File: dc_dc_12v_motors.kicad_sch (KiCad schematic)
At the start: 18 parts, among them Q7 CSD17505Q5A, Q8 CSD18540Q5B, U8 LM3150MH

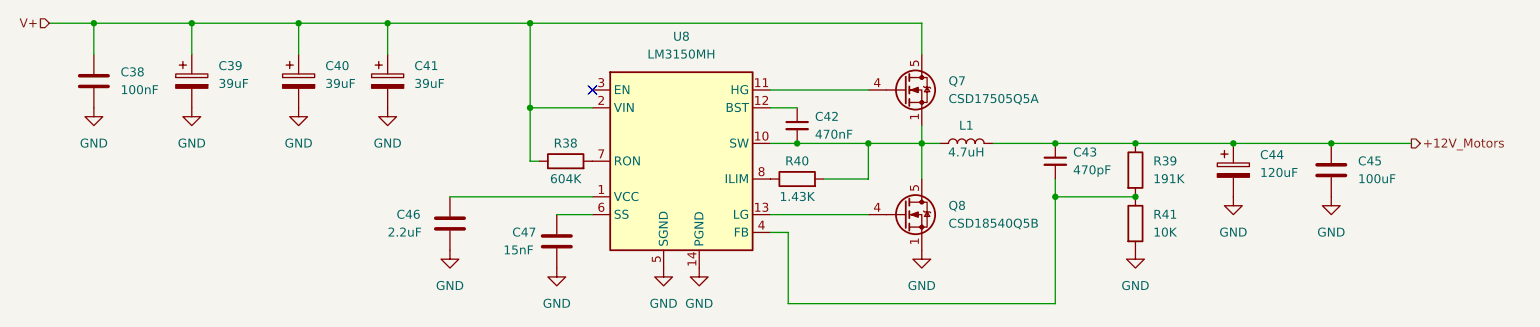
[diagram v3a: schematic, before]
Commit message: resolved all erc errors
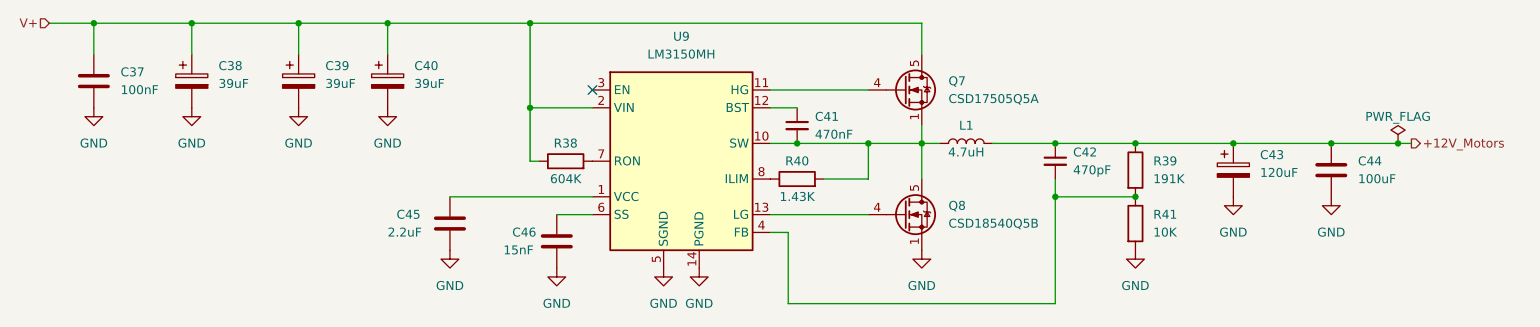
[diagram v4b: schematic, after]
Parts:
- renumbered C38 to C37, C39 to C38, C40 to C39, C41 to C40, C42 to C41, C43 to C42, C44 to C43, C45 to C44, C46 to C45, C47 to C46, U8 to U9
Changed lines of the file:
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@@
   (junction (at 222.885 91.44) (diameter 0) (color 0 0 0 0)
+  )
+  (junction (at 246.38 91.44) (diameter 0) (color 0 0 0 0)
   )
   (junction (at 102.235 74.295) (diameter 0) (color 0 0 0 0)
@@
     (stroke (width 0) (type default) (color 0 0 0 0))
   )
-  (wire (pts (xy 236.855 91.44) (xy 248.285 91.44))
+  (wire (pts (xy 236.855 91.44) (xy 246.38 91.44))
     (stroke (width 0) (type default) (color 0 0 0 0))
   )
@@
   )
   (wire (pts (xy 123.825 93.98) (xy 122.555 93.98))
+    (stroke (width 0) (type default) (color 0 0 0 0))
+  )
+  (wire (pts (xy 246.38 91.44) (xy 248.285 91.44))
     (stroke (width 0) (type default) (color 0 0 0 0))
   )
@@
   (symbol (lib_id "Device:C_Polarized") (at 222.885 95.25 0) (unit 1)
     (in_bom yes) (on_board yes) (fields_autoplaced)
-    (property "Reference" "C44" (id 0) (at 226.695 93.0909 0)
+    (property "Reference" "C43" (id 0) (at 226.695 93.0909 0)
       (effects (font (size 1.27 1.27)) (justify left))
     )
@@
   (symbol (lib_id "power:GND") (at 102.235 86.36 0) (unit 1)
     (in_bom yes) (on_board yes) (fields_autoplaced)
-    (property "Reference" "#PWR068" (id 0) (at 102.235 92.71 0)
+    (property "Reference" "#PWR064" (id 0) (at 102.235 92.71 0)
       (effects (font (size 1.27 1.27)) hide)
     )
@@
   (symbol (lib_id "power:GND") (at 222.885 99.06 0) (unit 1)
     (in_bom yes) (on_board yes) (fields_autoplaced)
-    (property "Reference" "#PWR069" (id 0) (at 222.885 105.41 0)
+    (property "Reference" "#PWR065" (id 0) (at 222.885 105.41 0)
       (effects (font (size 1.27 1.27)) hide)
     )
@@
   (symbol (lib_id "power:GND") (at 236.855 99.06 0) (unit 1)
     (in_bom yes) (on_board yes) (fields_autoplaced)
-    (property "Reference" "#PWR070" (id 0) (at 236.855 105.41 0)
+    (property "Reference" "#PWR066" (id 0) (at 236.855 105.41 0)
       (effects (font (size 1.27 1.27)) hide)
     )
@@
   (symbol (lib_id "Device:C_Small") (at 160.655 88.9 0) (unit 1)
     (in_bom yes) (on_board yes) (fields_autoplaced)
-    (property "Reference" "C42" (id 0) (at 163.195 87.6362 0)
+    (property "Reference" "C41" (id 0) (at 163.195 87.6362 0)
       (effects (font (size 1.27 1.27)) (justify left))
     )
@@
   (symbol (lib_id "power:GND") (at 208.915 106.68 0) (unit 1)
     (in_bom yes) (on_board yes) (fields_autoplaced)
-    (property "Reference" "#PWR073" (id 0) (at 208.915 113.03 0)
+    (property "Reference" "#PWR069" (id 0) (at 208.915 113.03 0)
       (effects (font (size 1.27 1.27)) hide)
     )
@@
   (symbol (lib_id "power:GND") (at 146.685 109.22 0) (unit 1)
     (in_bom yes) (on_board yes) (fields_autoplaced)
-    (property "Reference" "#PWR076" (id 0) (at 146.685 115.57 0)
+    (property "Reference" "#PWR072" (id 0) (at 146.685 115.57 0)
       (effects (font (size 1.27 1.27)) hide)
     )
@@
   (symbol (lib_id "Device:C") (at 111.125 102.87 0) (unit 1)
     (in_bom yes) (on_board yes)
-    (property "Reference" "C46" (id 0) (at 103.505 101.6 0)
+    (property "Reference" "C45" (id 0) (at 103.505 101.6 0)
       (effects (font (size 1.27 1.27)) (justify left))
     )
@@
   (symbol (lib_id "power:GND") (at 74.295 86.36 0) (unit 1)
     (in_bom yes) (on_board yes) (fields_autoplaced)
-    (property "Reference" "#PWR066" (id 0) (at 74.295 92.71 0)
+    (property "Reference" "#PWR062" (id 0) (at 74.295 92.71 0)
       (effects (font (size 1.27 1.27)) hide)
     )
@@
   (symbol (lib_id "Device:C") (at 60.325 82.55 0) (unit 1)
     (in_bom yes) (on_board yes) (fields_autoplaced)
-    (property "Reference" "C38" (id 0) (at 64.135 81.2799 0)
+    (property "Reference" "C37" (id 0) (at 64.135 81.2799 0)
       (effects (font (size 1.27 1.27)) (justify left))
     )
@@
   (symbol (lib_id "power:GND") (at 126.365 109.22 0) (unit 1)
     (in_bom yes) (on_board yes) (fields_autoplaced)
-    (property "Reference" "#PWR074" (id 0) (at 126.365 115.57 0)
+    (property "Reference" "#PWR070" (id 0) (at 126.365 115.57 0)
       (effects (font (size 1.27 1.27)) hide)
     )
@@
   (symbol (lib_id "power:GND") (at 89.535 86.36 0) (unit 1)
     (in_bom yes) (on_board yes) (fields_autoplaced)
-    (property "Reference" "#PWR067" (id 0) (at 89.535 92.71 0)
+    (property "Reference" "#PWR063" (id 0) (at 89.535 92.71 0)
       (effects (font (size 1.27 1.27)) hide)
     )
@@
   (symbol (lib_id "Device:C") (at 236.855 95.25 0) (unit 1)
     (in_bom yes) (on_board yes) (fields_autoplaced)
-    (property "Reference" "C45" (id 0) (at 240.665 93.9799 0)
+    (property "Reference" "C44" (id 0) (at 240.665 93.9799 0)
       (effects (font (size 1.27 1.27)) (justify left))
     )
@@
   (symbol (lib_id "Device:C_Small") (at 197.485 93.98 0) (unit 1)
     (in_bom yes) (on_board yes) (fields_autoplaced)
-    (property "Reference" "C43" (id 0) (at 200.025 92.7162 0)
+    (property "Reference" "C42" (id 0) (at 200.025 92.7162 0)
       (effects (font (size 1.27 1.27)) (justify left))
     )
@@
   (symbol (lib_id "Device:C_Polarized") (at 74.295 82.55 0) (unit 1)
     (in_bom yes) (on_board yes) (fields_autoplaced)
-    (property "Reference" "C39" (id 0) (at 78.105 80.3909 0)
+    (property "Reference" "C38" (id 0) (at 78.105 80.3909 0)
       (effects (font (size 1.27 1.27)) (justify left))
     )
@@
   (symbol (lib_id "Device:C_Polarized") (at 102.235 82.55 0) (unit 1)
     (in_bom yes) (on_board yes) (fields_autoplaced)
-    (property "Reference" "C41" (id 0) (at 106.045 80.3909 0)
+    (property "Reference" "C40" (id 0) (at 106.045 80.3909 0)
       (effects (font (size 1.27 1.27)) (justify left))
     )
@@
   (symbol (lib_id "Device:C_Polarized") (at 89.535 82.55 0) (unit 1)
     (in_bom yes) (on_board yes) (fields_autoplaced)
-    (property "Reference" "C40" (id 0) (at 93.345 80.3909 0)
+    (property "Reference" "C39" (id 0) (at 93.345 80.3909 0)
       (effects (font (size 1.27 1.27)) (justify left))
     )
@@
     (pin "2")
   )
+  (symbol (lib_id "power:PWR_FLAG") (at 246.38 91.44 0) (unit 1)
+    (in_bom yes) (on_board yes)
+    (property "Reference" "#FLG09" (id 0) (at 246.38 89.535 0)
+      (effects (font (size 1.27 1.27)) hide)
+    )
+    (property "Value" "PWR_FLAG" (id 1) (at 246.38 87.63 0))
+    (property "Footprint" "" (id 2) (at 246.38 91.44 0)
+      (effects (font (size 1.27 1.27)) hide)
+    )
+    (property "Datasheet" "~" (id 3) (at 246.38 91.44 0)
+      (effects (font (size 1.27 1.27)) hide)
+    )
+    (pin "1")
+  )
   (symbol (lib_id "Regulator_Switching:LM3150MH") (at 144.145 93.98 0) (unit 1)
     (in_bom yes) (on_board yes) (fields_autoplaced)
-    (property "Reference" "U8" (id 0) (at 144.145 76.2 0))
+    (property "Reference" "U9" (id 0) (at 144.145 76.2 0))
     (property "Value" "LM3150MH" (id 1) (at 144.145 78.74 0))
     (property "Footprint" "Package_SO:HTSSOP-14-1EP_4.4x5mm_P0.65mm_EP3.4x5mm_Mask3x3.1mm" (id 2) (at 146.685 107.95 0)
@@
   (symbol (lib_id "power:GND") (at 141.605 109.22 0) (unit 1)
     (in_bom yes) (on_board yes) (fields_autoplaced)
-    (property "Reference" "#PWR075" (id 0) (at 141.605 115.57 0)
+    (property "Reference" "#PWR071" (id 0) (at 141.605 115.57 0)
       (effects (font (size 1.27 1.27)) hide)
     )
@@
   (symbol (lib_id "power:GND") (at 111.125 106.68 0) (unit 1)
     (in_bom yes) (on_board yes) (fields_autoplaced)
-    (property "Reference" "#PWR071" (id 0) (at 111.125 113.03 0)
+    (property "Reference" "#PWR067" (id 0) (at 111.125 113.03 0)
       (effects (font (size 1.27 1.27)) hide)
     )
@@
   (symbol (lib_id "power:GND") (at 60.325 86.36 0) (unit 1)
     (in_bom yes) (on_board yes) (fields_autoplaced)
-    (property "Reference" "#PWR065" (id 0) (at 60.325 92.71 0)
+    (property "Reference" "#PWR061" (id 0) (at 60.325 92.71 0)
       (effects (font (size 1.27 1.27)) hide)
     )
@@
   (symbol (lib_id "power:GND") (at 178.435 106.68 0) (unit 1)
     (in_bom yes) (on_board yes) (fields_autoplaced)
-    (property "Reference" "#PWR072" (id 0) (at 178.435 113.03 0)
+    (property "Reference" "#PWR068" (id 0) (at 178.435 113.03 0)
       (effects (font (size 1.27 1.27)) hide)
     )
@@
   (symbol (lib_id "Device:C") (at 126.365 105.41 0) (unit 1)
     (in_bom yes) (on_board yes)
-    (property "Reference" "C47" (id 0) (at 120.015 104.14 0)
-      (effects (font (size 1.27 1.27)) (justify left))
-    )
+    (property "Reference" "C46" (id 0) (at 120.015 104.14 0)
+      (effects (font (size 1.27 1.27)) (justify left))
+    )

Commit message: updated footprints from schematics
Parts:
- C37: LCSC (none) -> C49678
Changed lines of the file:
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@@
+      (effects (font (size 1.27 1.27)) hide)
+    )
+    (property "LCSC" "C49678" (id 4) (at 60.325 82.55 0)
       (effects (font (size 1.27 1.27)) hide)
     )

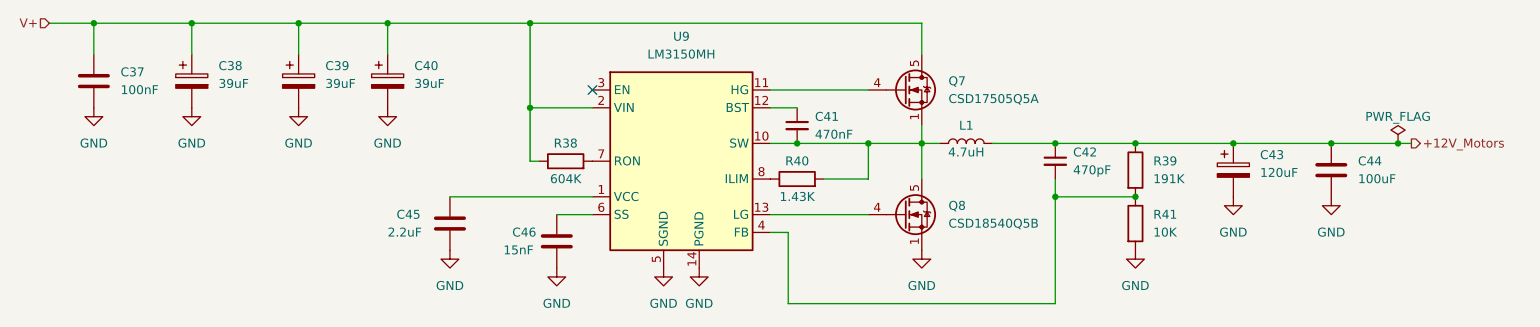
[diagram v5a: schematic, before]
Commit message: optimized component selection, assigned missing LCSC part numbers
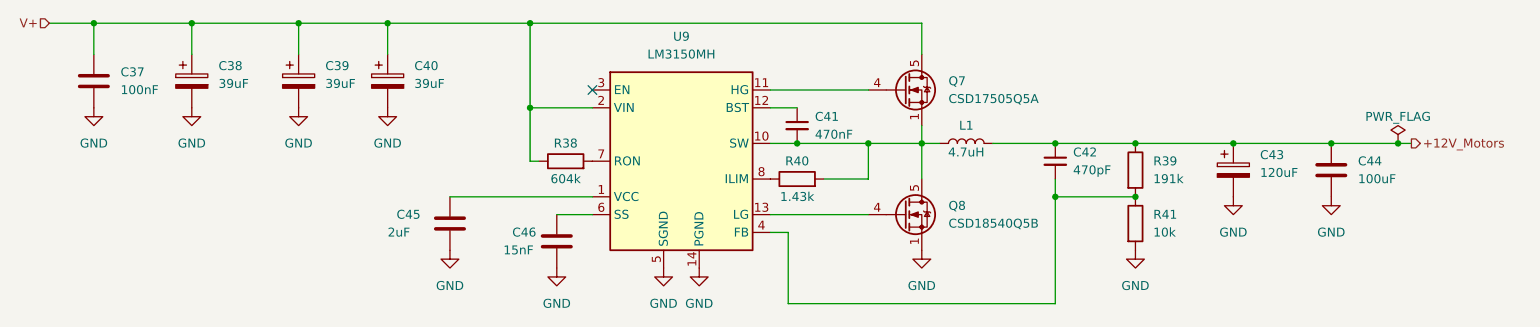
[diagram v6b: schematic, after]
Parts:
- C37: footprint Capacitor_SMD:C_0805_2012Metric_Pad1.18x1.45mm_HandSolder -> Capacitor_SMD:C_0805_2012Metric
- C38, C39, C40: LCSC (none) -> C189474
- C41: footprint Capacitor_SMD:C_0805_2012Metric_Pad1.18x1.45mm_HandSolder -> Capacitor_SMD:C_0805_2012Metric; LCSC (none) -> C13967
- C42: footprint Capacitor_SMD:C_0805_2012Metric_Pad1.18x1.45mm_HandSolder -> Capacitor_SMD:C_0805_2012Metric; LCSC (none) -> C1743
- C44: footprint Capacitor_SMD:C_1210_3225Metric_Pad1.33x2.70mm_HandSolder -> Capacitor_SMD:C_1210_3225Metric
- C45: value 2.2uF -> 2uF; footprint Capacitor_SMD:C_0805_2012Metric_Pad1.18x1.45mm_HandSolder -> Capacitor_SMD:C_0805_2012Metric; LCSC (none) -> C49217
- C46: footprint Capacitor_SMD:C_0805_2012Metric_Pad1.18x1.45mm_HandSolder -> Capacitor_SMD:C_0603_1608Metric; LCSC (none) -> C1596
- L1: LCSC (none) -> C2976965
- R38: value 604K -> 604k
- R39: value 191K -> 191k
- R40: value 1.43K -> 1.43k
- R41: value 10K -> 10k
- U9: LCSC (none) -> C48112
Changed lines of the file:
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@@
+      (effects (font (size 1.27 1.27)) hide)
+    )
+    (property "LCSC" "C2976965" (id 4) (at 184.785 91.44 0)
       (effects (font (size 1.27 1.27)) hide)
     )
@@
       (effects (font (size 1.27 1.27)) (justify left))
     )
-    (property "Footprint" "Capacitor_SMD:C_0805_2012Metric_Pad1.18x1.45mm_HandSolder" (id 2) (at 160.655 88.9 0)
-      (effects (font (size 1.27 1.27)) hide)
-    )
-    (property "Datasheet" "~" (id 3) (at 160.655 88.9 0)
+    (property "Footprint" "Capacitor_SMD:C_0805_2012Metric" (id 2) (at 160.655 88.9 0)
+      (effects (font (size 1.27 1.27)) hide)
+    )
+    (property "Datasheet" "https://datasheet.lcsc.com/lcsc/1810251812_Samsung-Electro-Mechanics-CL21B474KBFNNNE_C13967.pdf" (id 3) (at 160.655 88.9 0)
+      (effects (font (size 1.27 1.27)) hide)
+    )
+    (property "LCSC" "C13967" (id 4) (at 160.655 88.9 0)
       (effects (font (size 1.27 1.27)) hide)
     )
@@
     (in_bom yes) (on_board yes)
     (property "Reference" "R40" (id 0) (at 160.655 93.98 90))
-    (property "Value" "1.43K" (id 1) (at 160.655 99.06 90))
+    (property "Value" "1.43k" (id 1) (at 160.655 99.06 90))
     (property "Footprint" "Resistor_SMD:R_0805_2012Metric_Pad1.20x1.40mm_HandSolder" (id 2) (at 160.655 98.298 90)
       (effects (font (size 1.27 1.27)) hide)
@@
       (effects (font (size 1.27 1.27)) (justify left))
     )
-    (property "Value" "2.2uF" (id 1) (at 102.235 104.14 0)
-      (effects (font (size 1.27 1.27)) (justify left))
-    )
-    (property "Footprint" "Capacitor_SMD:C_0805_2012Metric_Pad1.18x1.45mm_HandSolder" (id 2) (at 112.0902 106.68 0)
-      (effects (font (size 1.27 1.27)) hide)
-    )
-    (property "Datasheet" "~" (id 3) (at 111.125 102.87 0)
+    (property "Value" "2uF" (id 1) (at 102.235 104.14 0)
+      (effects (font (size 1.27 1.27)) (justify left))
+    )
+    (property "Footprint" "Capacitor_SMD:C_0805_2012Metric" (id 2) (at 112.0902 106.68 0)
+      (effects (font (size 1.27 1.27)) hide)
+    )
+    (property "Datasheet" "https://datasheet.lcsc.com/lcsc/1811101411_FH--Guangdong-Fenghua-Advanced-Tech-0805F225M500NT_C49217.pdf" (id 3) (at 111.125 102.87 0)
+      (effects (font (size 1.27 1.27)) hide)
+    )
+    (property "LCSC" "C49217" (id 4) (at 111.125 102.87 0)
       (effects (font (size 1.27 1.27)) hide)
     )
@@
       (effects (font (size 1.27 1.27)) (justify left))
     )
-    (property "Footprint" "Capacitor_SMD:C_0805_2012Metric_Pad1.18x1.45mm_HandSolder" (id 2) (at 61.2902 86.36 0)
+    (property "Footprint" "Capacitor_SMD:C_0805_2012Metric" (id 2) (at 61.2902 86.36 0)
       (effects (font (size 1.27 1.27)) hide)
     )
@@
       (effects (font (size 1.27 1.27)) (justify left))
     )
-    (property "Footprint" "Capacitor_SMD:C_1210_3225Metric_Pad1.33x2.70mm_HandSolder" (id 2) (at 237.8202 99.06 0)
+    (property "Footprint" "Capacitor_SMD:C_1210_3225Metric" (id 2) (at 237.8202 99.06 0)
       (effects (font (size 1.27 1.27)) hide)
     )
@@
       (effects (font (size 1.27 1.27)) (justify left))
     )
-    (property "Footprint" "Capacitor_SMD:C_0805_2012Metric_Pad1.18x1.45mm_HandSolder" (id 2) (at 197.485 93.98 0)
-      (effects (font (size 1.27 1.27)) hide)
-    )
-    (property "Datasheet" "~" (id 3) (at 197.485 93.98 0)
+    (property "Footprint" "Capacitor_SMD:C_0805_2012Metric" (id 2) (at 197.485 93.98 0)
+      (effects (font (size 1.27 1.27)) hide)
+    )
+    (property "Datasheet" "https://datasheet.lcsc.com/lcsc/1811110920_FH--Guangdong-Fenghua-Advanced-Tech-0805B471K500NT_C1743.pdf" (id 3) (at 197.485 93.98 0)
+      (effects (font (size 1.27 1.27)) hide)
+    )
+    (property "LCSC" "C1743" (id 4) (at 197.485 93.98 0)
       (effects (font (size 1.27 1.27)) hide)
     )
@@
     (in_bom yes) (on_board yes)
     (property "Reference" "R38" (id 0) (at 127.635 91.44 90))
-    (property "Value" "604K" (id 1) (at 127.635 96.52 90))
+    (property "Value" "604k" (id 1) (at 127.635 96.52 90))
     (property "Footprint" "Resistor_SMD:R_0805_2012Metric_Pad1.20x1.40mm_HandSolder" (id 2) (at 127.635 95.758 90)
       (effects (font (size 1.27 1.27)) hide)
@@
       (effects (font (size 1.27 1.27)) hide)
     )
+    (property "LCSC" "C189474" (id 4) (at 74.295 82.55 0)
+      (effects (font (size 1.27 1.27)) hide)
+    )
     (pin "1")
     (pin "2")
@@
       (effects (font (size 1.27 1.27)) hide)
     )
+    (property "LCSC" "C189474" (id 4) (at 102.235 82.55 0)
+      (effects (font (size 1.27 1.27)) hide)
+    )
     (pin "1")
     (pin "2")
@@
       (effects (font (size 1.27 1.27)) hide)
     )
+    (property "LCSC" "C189474" (id 4) (at 89.535 82.55 0)
+      (effects (font (size 1.27 1.27)) hide)
+    )
     (pin "1")
     (pin "2")
@@
       (effects (font (size 1.27 1.27)) (justify left))
     )
-    (property "Value" "191K" (id 1) (at 211.455 96.5199 0)
+    (property "Value" "191k" (id 1) (at 211.455 96.5199 0)
       (effects (font (size 1.27 1.27)) (justify left))
     )
@@
     )
     (property "Datasheet" "http://www.ti.com/lit/ds/symlink/lm3150.pdf" (id 3) (at 194.945 105.41 0)
+      (effects (font (size 1.27 1.27)) hide)
+    )
+    (property "LCSC" "C48112" (id 4) (at 144.145 93.98 0)
       (effects (font (size 1.27 1.27)) hide)
     )
@@
       (effects (font (size 1.27 1.27)) (justify left))
     )
-    (property "Footprint" "Capacitor_SMD:C_0805_2012Metric_Pad1.18x1.45mm_HandSolder" (id 2) (at 127.3302 109.22 0)
-      (effects (font (size 1.27 1.27)) hide)
-    )
-    (property "Datasheet" "~" (id 3) (at 126.365 105.41 0)
+    (property "Footprint" "Capacitor_SMD:C_0603_1608Metric" (id 2) (at 127.3302 109.22 0)
+      (effects (font (size 1.27 1.27)) hide)
+    )
+    (property "Datasheet" "https://datasheet.lcsc.com/lcsc/1811061810_FH--Guangdong-Fenghua-Advanced-Tech-0603B153K500NT_C1596.pdf" (id 3) (at 126.365 105.41 0)
+      (effects (font (size 1.27 1.27)) hide)
+    )
+    (property "LCSC" "C1596" (id 4) (at 126.365 105.41 0)
       (effects (font (size 1.27 1.27)) hide)
     )
@@
       (effects (font (size 1.27 1.27)) (justify left))
     )
-    (property "Value" "10K" (id 1) (at 211.455 104.1399 0)
-      (effects (font (size 1.27 1.27)) (justify left))
-    )
+    (property "Value" "10k" (id 1) (at 211.455 104.1399 0)
+      (effects (font (size 1.27 1.27)) (justify left))
+    )
